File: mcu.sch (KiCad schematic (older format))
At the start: 62 parts, among them J11 RJ45_Shielded, J13 HR911105A, J2 RJ45_Shielded, U3 STM32F207VGT6, U4 MCP2562-E-P, U5 LAN8720A, Y1 Crystal_GND24

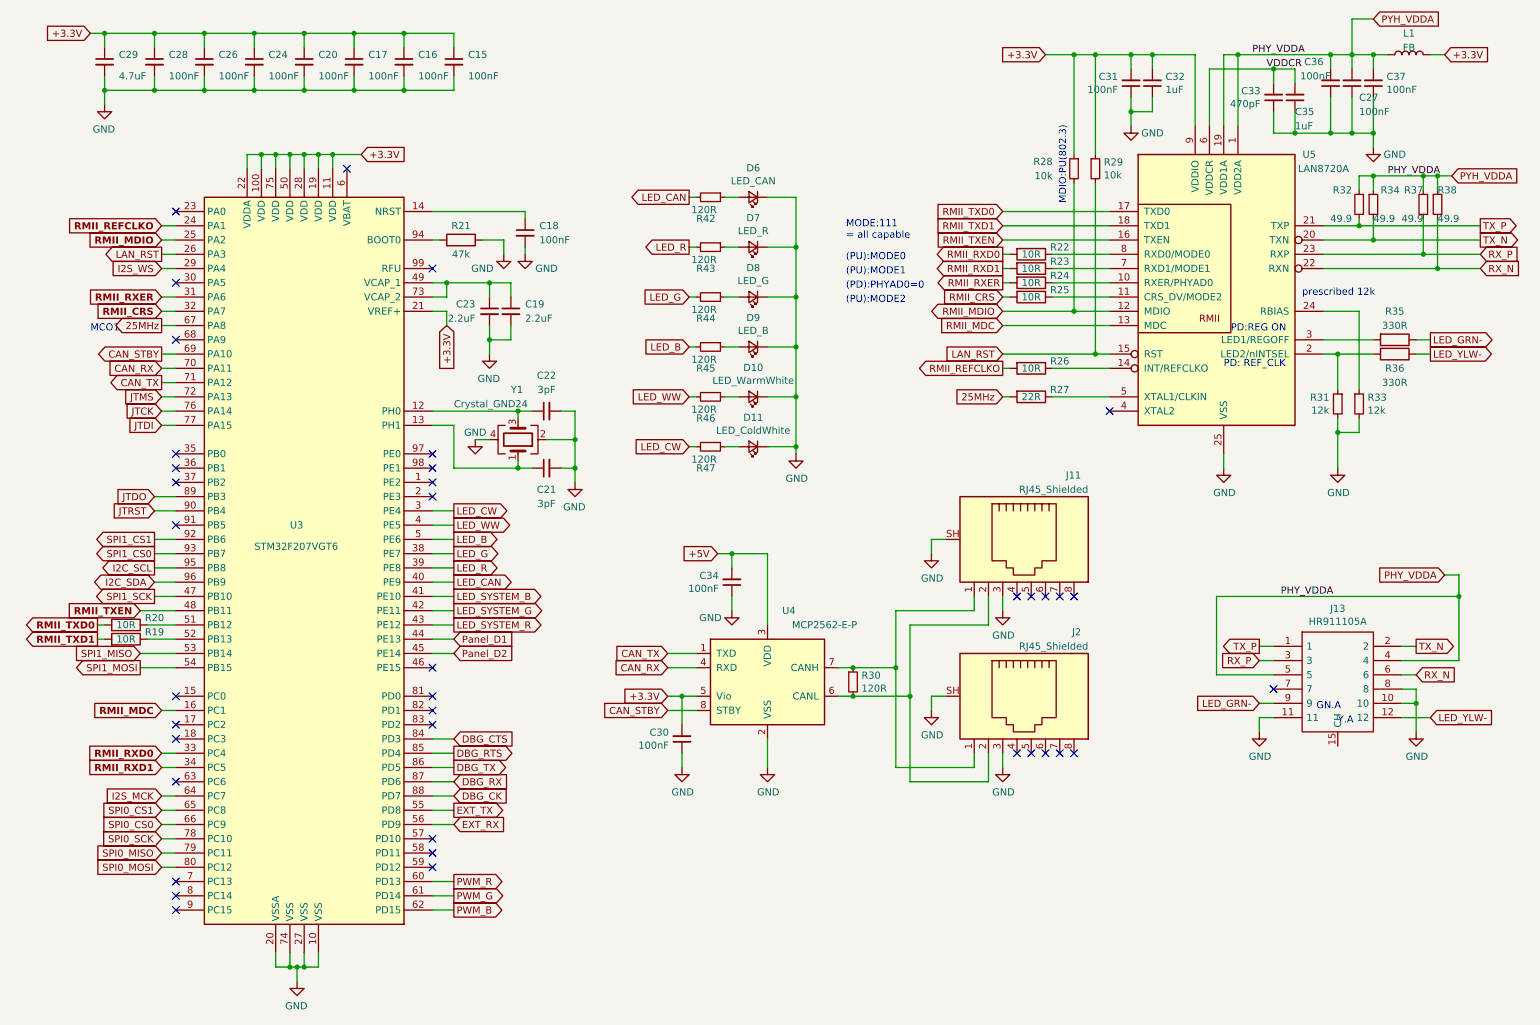
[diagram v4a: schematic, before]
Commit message: THT pad restring sizes increase for mechanical stability; generalized LED arrangement for more flexibility (8 bit display, CAN LED, PWM and general purpose RGB) and development-style look and feel; protection diode footprint is now THT to reduce reworking hassle should it short out due to misuse
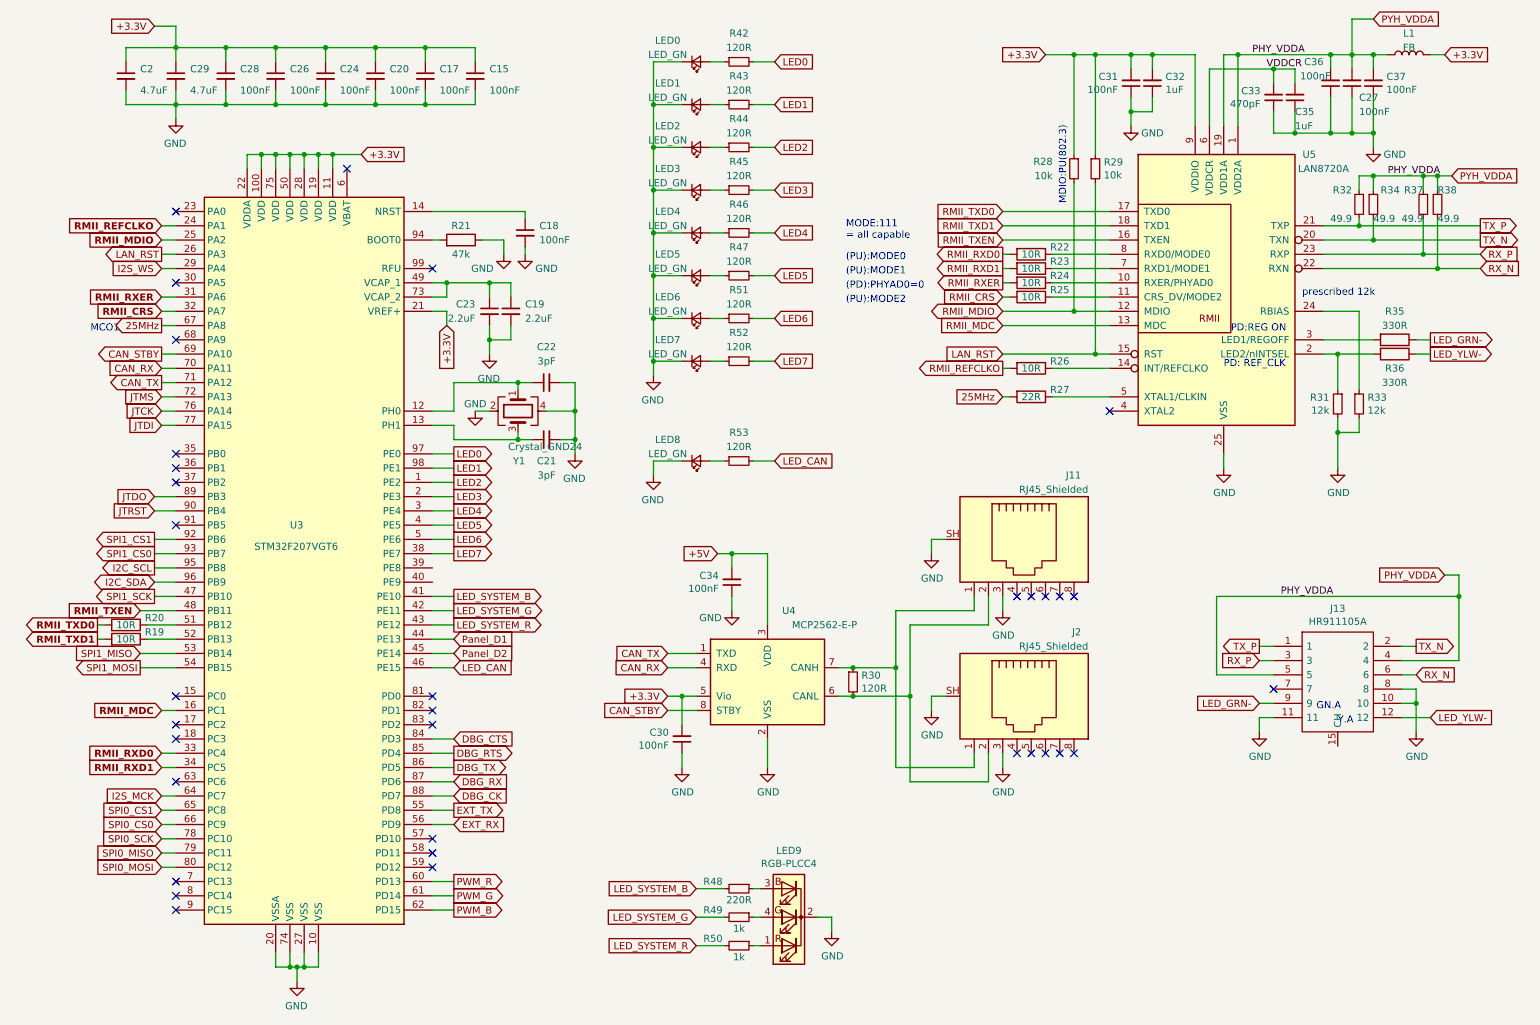
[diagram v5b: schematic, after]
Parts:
- removed C16: 100nF, Capacitor_SMD:C_0603_1608Metric, symbol Device:C_Small
- removed D10: LED_WarmWhite, LED_SMD:LED_0603_1608Metric_Castellated, symbol Device:LED_Small
- removed D11: LED_ColdWhite, LED_SMD:LED_0603_1608Metric_Castellated, symbol Device:LED_Small
- removed D7: LED_R, LED_SMD:LED_0603_1608Metric_Castellated, symbol Device:LED_Small
- removed D8: LED_G, LED_SMD:LED_0603_1608Metric_Castellated, symbol Device:LED_Small
- removed D9: LED_B, LED_SMD:LED_0603_1608Metric_Castellated, symbol Device:LED_Small
- added C2: 4.7uF, Capacitor_SMD:C_0805_2012Metric, symbol Device:C_Small
- added LED1, LED2, LED3, LED4, LED5, LED6, LED7, LED8: LED_GN, LED_SMD:LED_0603_1608Metric_Castellated, symbol Device:LED_Small
- added LED9: RGB-PLCC4, LED_SMD:LED_Cree-PLCC4_2x2mm_CW, symbol Device:LED_RCBG
- added R48: 220R, Resistor_SMD:R_0603_1608Metric, symbol Device:R_Small
- added R49, R50: 1k, Resistor_SMD:R_0603_1608Metric, symbol Device:R_Small
- added R51, R52, R53: 120R, Resistor_SMD:R_0603_1608Metric, symbol Device:R_Small
- C29: footprint Capacitor_SMD:C_0603_1608Metric -> Capacitor_SMD:C_0805_2012Metric
- LED0: renamed from D6; value LED_CAN -> LED_GN
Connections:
- net +3.3V: now also C2.1
- net GND: now also C2.2, LED1.1 (K), LED2.1 (K), LED3.1 (K), LED4.1 (K), LED5.1 (K), LED6.1 (K), LED7.1 (K), LED8.1 (K), LED9.2 (K)
- net LED_CAN: now also U3.46 (PE15), R53.2; no longer R42.2, U3.40 (PE9)
- net LED_SYSTEM_B: now also R48.2
- net LED_SYSTEM_G: now also R49.2
- net LED_SYSTEM_R: now also R50.2
- net LED2: now reaches U3.1 (PE2)
- net LED2: now also R44.2
- net at C22.1, U3.12 (PH0): now also Y1.1; no longer Y1.3
- net at C21.1, U3.13 (PH1): now also Y1.3; no longer Y1.1
- net LED3: now reaches U3.2 (PE3)
- net LED3: now also R45.2
- net LED0: now reaches U3.97 (PE0)
- net LED0: now also R42.2
- net LED1: now reaches U3.98 (PE1)
- net LED1: now also R43.2
- net at R43.1: now also LED1.2 (A)
- net at R46.1: now also LED4.2 (A)
- net at R47.1: now also LED5.2 (A)
- net at R44.1: now also LED2.2 (A)
- net at R45.1: now also LED3.2 (A)
- net LED_B renamed LED6
- net LED6: now also R51.2; no longer R45.2
- net LED_CW renamed LED4
- net LED4: now also R46.2; no longer R47.2
- net LED_G renamed LED7
- net LED7: now also R52.2; no longer R44.2
- net LED_R: no longer names the net of U3.39 (PE8)
- net LED_R: no longer R43.2
- net LED_WW renamed LED5
- net LED5: now also R47.2; no longer R46.2
- new net: LED9.1 (RA), R50.1
- new net: LED9.3 (BA), R48.1
- new net: LED9.4 (GA), R49.1
- new net: LED6.2 (A), R51.1
- new net: LED7.2 (A), R52.1
- new net: LED8.2 (A), R53.1
- no-connect marks 39 -> 34
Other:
- moved on the sheet: C15, C17, C20, C21, C22, C24, C26, C28, C29, LED0, R42, Y1

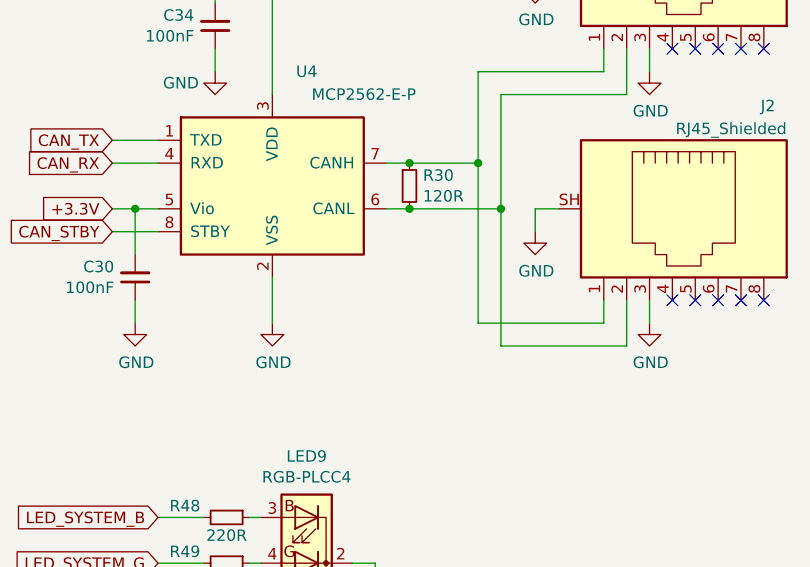
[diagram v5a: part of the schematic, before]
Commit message: add CAN termination jumper, switch-mode DCDC power routing and current sink routing done. Barrel jacks still need swapping?
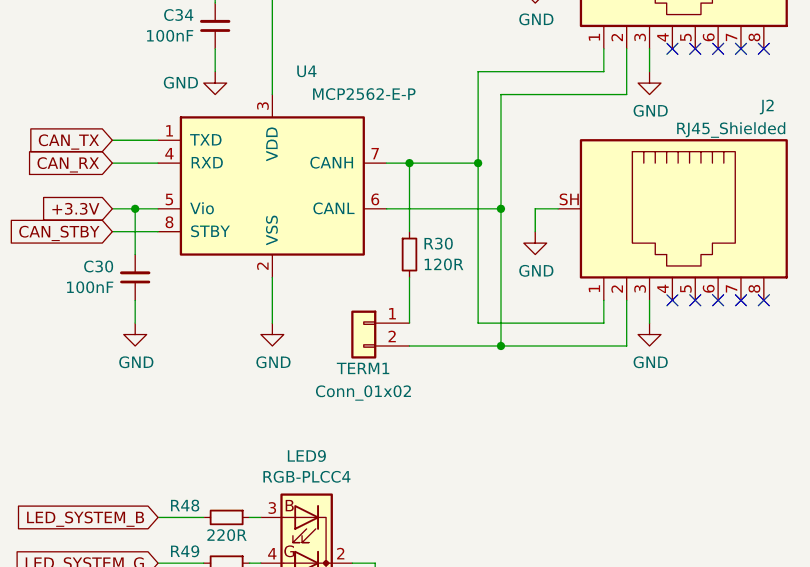
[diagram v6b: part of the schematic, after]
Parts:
- added TERM1: Conn_01x02, Connector_PinHeader_2.00mm:PinHeader_1x02_P2.00mm_Vertical, symbol Connector_Generic:Conn_01x02
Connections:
- net at J11.2, J2.2, U4.6 (CANL): now also TERM1.2 (Pin_2); no longer R30.2
- new net: R30.2, TERM1.1 (Pin_1)
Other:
- moved on the sheet: R30
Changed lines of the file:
@@
 Wire Wire Line
 	5050 5500 5250 5500
-Wire Wire Line
-	6250 5200 6350 5200
-Wire Wire Line
-	6250 5400 6350 5400
 $Comp
 L Device:C_Small C34
@@
 L Device:R_Small R30
 U 1 1 5BBE7B3D
-P 6350 5300
+P 6350 5600
 AR Path="/5BBC4BB7/5BBE7B3D" Ref="R30"  Part="1"
 AR Path="/5C1EFDBE/5BBE7B3D" Ref="R?"  Part="1"
 AR Path="/5C211DD3/5BBE7B3D" Ref="R?"  Part="1"
 AR Path="/5C211FC6/5BBE7B3D" Ref="R?"  Part="1"
-F 0 "R30" H 6409 5346 50  0000 L CNN
-F 1 "120R" H 6409 5255 50  0000 L CNN
-F 2 "Resistor_SMD:R_0603_1608Metric" H 6350 5300 50  0001 C CNN
-F 3 "~" H 6350 5300 50  0001 C CNN
-	1    6350 5300
+F 0 "R30" H 6409 5646 50  0000 L CNN
+F 1 "120R" H 6409 5555 50  0000 L CNN
+F 2 "Resistor_SMD:R_0603_1608Metric" H 6350 5600 50  0001 C CNN
+F 3 "~" H 6350 5600 50  0001 C CNN
+	1    6350 5600
 	1    0    0    -1
 $EndComp
@@
 Wire Wire Line
 	7400 4700 7400 4800
-Wire Wire Line
-	6350 5200 6650 5200
-Connection ~ 6350 5200
 Connection ~ 6650 5200
 Wire Wire Line
 	6650 5200 6650 5900
-Wire Wire Line
-	6350 5400 6750 5400
-Connection ~ 6350 5400
 Connection ~ 6750 5400
 Wire Wire Line
@@
 	4950 3150 4950 3050
 Connection ~ 4950 3050
+Wire Wire Line
+	6250 5400 6750 5400
+Wire Wire Line
+	6250 5200 6350 5200
+Wire Wire Line
+	6350 5500 6350 5200
+Connection ~ 6350 5200
+Wire Wire Line
+	6350 5200 6650 5200
+$Comp
+L Connector_Generic:Conn_01x02 TERM1
+U 1 1 5BDBFB79
+P 6150 5900
+F 0 "TERM1" H 6150 5700 50  0000 C CNN
+F 1 "Conn_01x02" H 6150 5600 50  0000 C CNN
+F 2 "Connector_PinHeader_2.00mm:PinHeader_1x02_P2.00mm_Vertical" H 6150 5900 50  0001 C CNN
+F 3 "~" H 6150 5900 50  0001 C CNN
+	1    6150 5900
+	-1   0    0    -1
+$EndComp
+Wire Wire Line
+	6350 5700 6350 5900
+Wire Wire Line
+	6350 6000 6750 6000
+Connection ~ 6750 6000
 $EndSCHEMATC

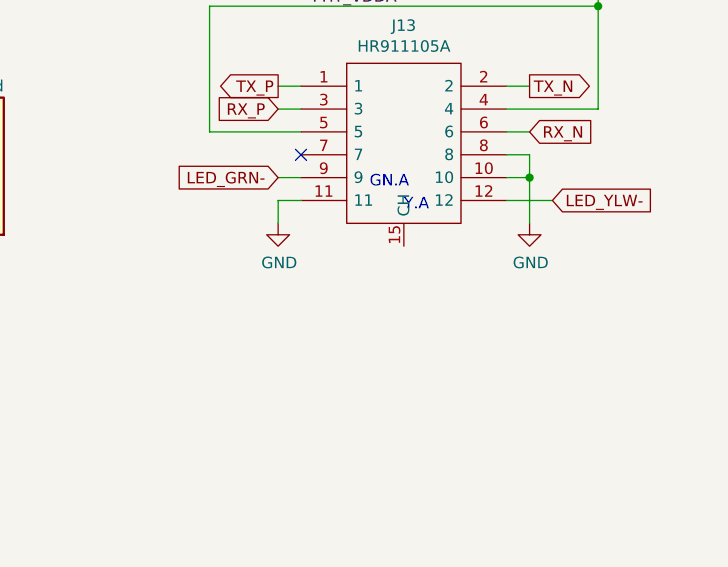
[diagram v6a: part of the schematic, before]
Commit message: all connector shields are now connected to ground. Note HR911105A LED pins are offset by 4.9mm whereas the WE LED pins are at 4.1mm. Can still fit the WE part? but it won't be pretty.
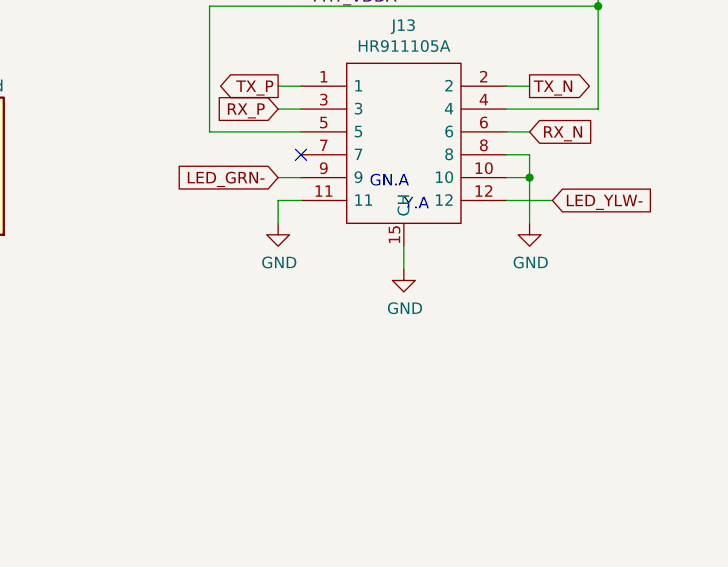
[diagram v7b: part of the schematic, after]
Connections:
- net GND: now also J13.15 (CH), J13.16 (CH)
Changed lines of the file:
@@
 	6350 6000 6750 6000
 Connection ~ 6750 6000
+$Comp
+L power:GND #PWR0132
+U 1 1 5BE6B640
+P 9750 5850
+AR Path="/5BBC4BB7/5BE6B640" Ref="#PWR0132"  Part="1"
+AR Path="/5C1EFDBE/5BE6B640" Ref="#PWR?"  Part="1"
+AR Path="/5C211DD3/5BE6B640" Ref="#PWR?"  Part="1"
+AR Path="/5C211FC6/5BE6B640" Ref="#PWR?"  Part="1"
+F 0 "#PWR0132" H 9750 5600 50  0001 C CNN
+F 1 "GND" H 9755 5677 50  0000 C CNN
+F 2 "" H 9750 5850 50  0001 C CNN
+F 3 "" H 9750 5850 50  0001 C CNN
+	1    9750 5850
+	1    0    0    -1
+$EndComp
+Wire Wire Line
+	9750 5850 9750 5750
 $EndSCHEMATC

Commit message: lots of labels!
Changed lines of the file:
@@
 L power:GND #PWR0107
 U 1 1 5BEECAF4
-P 9200 5650
+P 9200 5850
 AR Path="/5BBC4BB7/5BEECAF4" Ref="#PWR0107"  Part="1"
 AR Path="/5C1EFDBE/5BEECAF4" Ref="#PWR?"  Part="1"
 AR Path="/5C211DD3/5BEECAF4" Ref="#PWR?"  Part="1"
 AR Path="/5C211FC6/5BEECAF4" Ref="#PWR?"  Part="1"
-F 0 "#PWR0107" H 9200 5400 50  0001 C CNN
-F 1 "GND" H 9205 5477 50  0000 C CNN
-F 2 "" H 9200 5650 50  0001 C CNN
-F 3 "" H 9200 5650 50  0001 C CNN
-	1    9200 5650
+F 0 "#PWR0107" H 9200 5600 50  0001 C CNN
+F 1 "GND" H 9205 5677 50  0000 C CNN
+F 2 "" H 9200 5850 50  0001 C CNN
+F 3 "" H 9200 5850 50  0001 C CNN
+	1    9200 5850
 	1    0    0    -1
 $EndComp
@@
 	10450 1750 10550 1750
 Wire Wire Line
-	9200 5550 9200 5650
+	9200 5550 9200 5850
 $Comp
 L power:GND #PWR029
 U 1 1 5E8581A9
-P 10300 5650
+P 10300 5850
 AR Path="/5BBC4BB7/5E8581A9" Ref="#PWR029"  Part="1"
 AR Path="/5C1EFDBE/5E8581A9" Ref="#PWR?"  Part="1"
 AR Path="/5C211DD3/5E8581A9" Ref="#PWR?"  Part="1"
 AR Path="/5C211FC6/5E8581A9" Ref="#PWR?"  Part="1"
-F 0 "#PWR029" H 10300 5400 50  0001 C CNN
-F 1 "GND" H 10305 5477 50  0000 C CNN
-F 2 "" H 10300 5650 50  0001 C CNN
-F 3 "" H 10300 5650 50  0001 C CNN
-	1    10300 5650
+F 0 "#PWR029" H 10300 5600 50  0001 C CNN
+F 1 "GND" H 10305 5677 50  0000 C CNN
+F 2 "" H 10300 5850 50  0001 C CNN
+F 3 "" H 10300 5850 50  0001 C CNN
+	1    10300 5850
 	1    0    0    -1
 $EndComp
 Wire Wire Line
-	10300 5450 10300 5650
+	10300 5450 10300 5850
 Connection ~ 10300 5450
 Text Label 9250 1000 0    50   ~ 0
